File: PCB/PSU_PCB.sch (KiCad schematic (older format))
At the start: 127 parts, among them CON1 BARREL_JACK, IC1 ATMEGA328-P, P1 USB_OTG, P2 FTDI, P3 V+, P4 V-, P5 ISP, P6 I2C, P7 LCD_Display, Q1 TIP32CG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

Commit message: Small schematic fixes + added backpanel design
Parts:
- removed R37: 1.8k, Resistors_ThroughHole:Resistor_Horizontal_RM10mm, symbol R
- added D8: SS34, Diodes_SMD:D_SMB_Handsoldering, symbol D_Schottky
- D3: footprint Resistors_ThroughHole:Resistor_Horizontal_RM15mm -> Diodes_ThroughHole:D_DO-15_P15.24mm_Horizontal
- R28: value 1.8k -> 2.2k
- R39: value 1k -> 100R
- R48: value 1.8k -> 2.2k; footprint Resistors_ThroughHole:R_Axial_DIN0204_L3.6mm_D1.6mm_P7.62mm_Horizontal -> Resistors_ThroughHole:R_Axial_DIN0207_L6.3mm_D2.5mm_P10.16mm_Horizontal
- R50: value 1k -> 620R
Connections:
- net GND: now also Q2.1 (E)
- net VEE: no longer Q2.1 (E)
- net at BT1.1, R27.2, SW1.1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: now also D8.1 (K); no longer Q1.2 (C)
- new net: D8.2 (A), Q1.2 (C)
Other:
- note added: "(R50+Rpot)//R48"
- note added: "1.46 - 2.05 V"
- note added: "8 - 24 V"
- note added: "8 - 24 V\n"
- note added: "R51"
- note added: "Tab \nBAT"
- note added: "VCC max = 15 V\nTie TS to VCC/2 \nto disable temp \nmonitoring"
- note added: "Vboost=1.25(1+ )"
- note added: "__________________"
- note removed: "-3,3V"
- note removed: "1.25 - 1.75 V"
- note removed: "9 - 22 V"
- note removed: "9 - 22 V\n"
- note removed: ">650R\n<1.55K\n"
- note removed: "Off: Vout = 0 V\nVgate < 0.6 V \n"
- note removed: "VCC max = 15 V\nTie VS to VCC/2 \nto disable temp \nmonitoring"
- moved on the sheet: C24, C25, Q1, R48, R50, R51, R6, U10

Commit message: Updated BOM
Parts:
- C21: footprint Capacitors_ThroughHole:C_Disc_D3.0mm_W1.6mm_P2.50mm -> Capacitors_ThroughHole:C_Rect_L7.0mm_W2.5mm_P5.00mm
- D9: renamed from 1N4007; value D -> 1N4007
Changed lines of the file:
@@
 8E D2 4E 06 E9 83 31 0C B8 01 D4 62 7A FA FE CA 1E E7 AB A8 50 4D B8 D1 52 86 A6 EF 44 4C F7 6B
 69 A6 CB 4C 71 E1 73 B8 2B 4F 00 E7 75 28 F9 2E A2 C6 63 AC 40 DB 07 B2 19 61 39 9A 3C 4A F1 B4
-F5 AD 2E B3 0D FC 7F 6D 80 3F 3C 28 70 B1 D5 00 00 00 00 49 45 4E 44 AE 42 60 82 D3
+F5 AD 2E B3 0D FC 7F 6D 80 3F 3C 28 70 B1 D5 00 00 00 00 49 45 4E 44 AE 42 60 82 D1
 EndData
 $EndBitmap
 $Comp
-L D 1N4007
+L D D9
 U 1 1 57F00E00
 P 4200 650
-F 0 "1N4007" H 4200 750 50  0000 C CNN
-F 1 "D" H 4200 550 50  0000 C CNN
+F 0 "D9" H 4200 750 50  0000 C CNN
+F 1 "1N4007" H 4200 550 50  0000 C CNN
 F 2 "Diodes_ThroughHole:D_DO-41_SOD81_P10.16mm_Horizontal" H 4200 650 50  0001 C CNN
 F 3 "" H 4200 650 50  0000 C CNN
@@
 F 0 "C21" H 9310 5120 50  0000 L CNN
 F 1 "100n" H 9300 5000 50  0000 L CNN
-F 2 "Capacitors_ThroughHole:C_Disc_D3.0mm_W1.6mm_P2.50mm" H 9300 5050 50  0001 C CNN
+F 2 "Capacitors_ThroughHole:C_Rect_L7.0mm_W2.5mm_P5.00mm" H 9300 5050 50  0001 C CNN
 F 3 "" H 9300 5050 50  0000 C CNN
 	1    9300 5050
@@
 00 09 E8 04 41 10 04 61 00 48 40 27 08 82 20 08 03 40 02 3A 41 10 04 41 18 00 23 00 F5 5D DD 09
 82 20 08 82 20 B4 52 CF 06 60 0D 60 1C 9A D7 A4 13 04 41 10 04 D1 BD 50 00 7E F8 7F 36 C9 A5 48
-A4 FE A8 58 00 00 00 00 49 45 4E 44 AE 42 60 82 E0
+A4 FE A8 58 00 00 00 00 49 45 4E 44 AE 42 60 82 C0
 EndData
 $EndBitmap

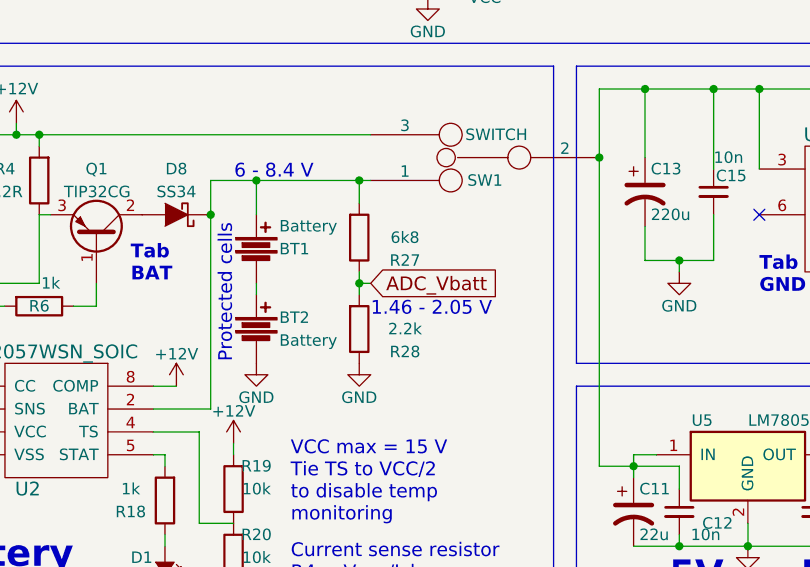
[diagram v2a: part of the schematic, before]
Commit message: Changed battery monitor resistors
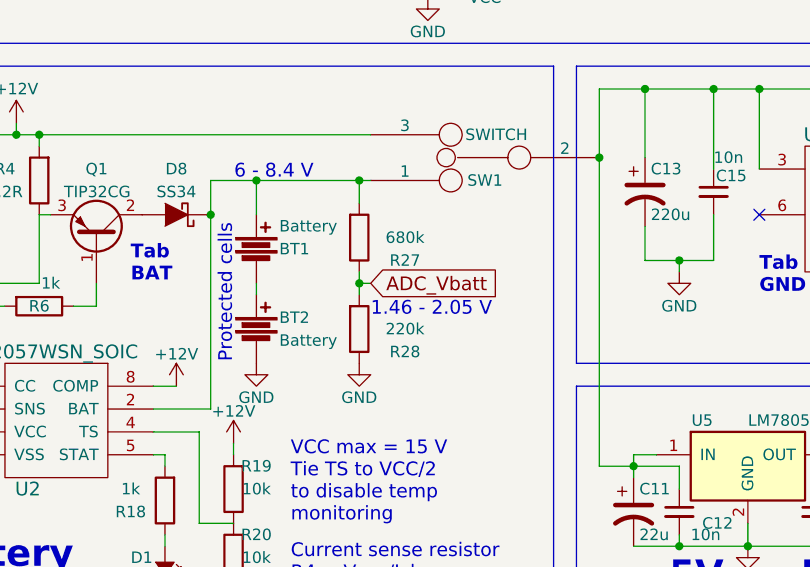
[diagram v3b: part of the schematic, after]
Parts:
- R27: value 6k8 -> 680k
- R28: value 2.2k -> 220k
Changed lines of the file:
@@
 P 2950 6350
 F 0 "R28" H 3150 6450 50  0000 C CNN
-F 1 "2.2k" H 3150 6350 50  0000 C CNN
+F 1 "220k" H 3150 6350 50  0000 C CNN
 F 2 "Resistors_ThroughHole:Resistor_Horizontal_RM10mm" V 2880 6350 50  0001 C CNN
 F 3 "" H 2950 6350 50  0000 C CNN
@@
 P 2950 5950
 F 0 "R27" H 3150 6050 50  0000 C CNN
-F 1 "6k8" H 3150 5950 50  0000 C CNN
+F 1 "680k" H 3150 5950 50  0000 C CNN
 F 2 "Resistors_ThroughHole:Resistor_Horizontal_RM10mm" V 2880 5950 50  0001 C CNN
 F 3 "" H 2950 5950 50  0000 C CNN
@@
 8E D2 4E 06 E9 83 31 0C B8 01 D4 62 7A FA FE CA 1E E7 AB A8 50 4D B8 D1 52 86 A6 EF 44 4C F7 6B
 69 A6 CB 4C 71 E1 73 B8 2B 4F 00 E7 75 28 F9 2E A2 C6 63 AC 40 DB 07 B2 19 61 39 9A 3C 4A F1 B4
-F5 AD 2E B3 0D FC 7F 6D 80 3F 3C 28 70 B1 D5 00 00 00 00 49 45 4E 44 AE 42 60 82 D1
+F5 AD 2E B3 0D FC 7F 6D 80 3F 3C 28 70 B1 D5 00 00 00 00 49 45 4E 44 AE 42 60 82 43
 EndData
 $EndBitmap
@@
 00 09 E8 04 41 10 04 61 00 48 40 27 08 82 20 08 03 40 02 3A 41 10 04 41 18 00 23 00 F5 5D DD 09
 82 20 08 82 20 B4 52 CF 06 60 0D 60 1C 9A D7 A4 13 04 41 10 04 D1 BD 50 00 7E F8 7F 36 C9 A5 48
-A4 FE A8 58 00 00 00 00 49 45 4E 44 AE 42 60 82 C0
+A4 FE A8 58 00 00 00 00 49 45 4E 44 AE 42 60 82 90
 EndData
 $EndBitmap

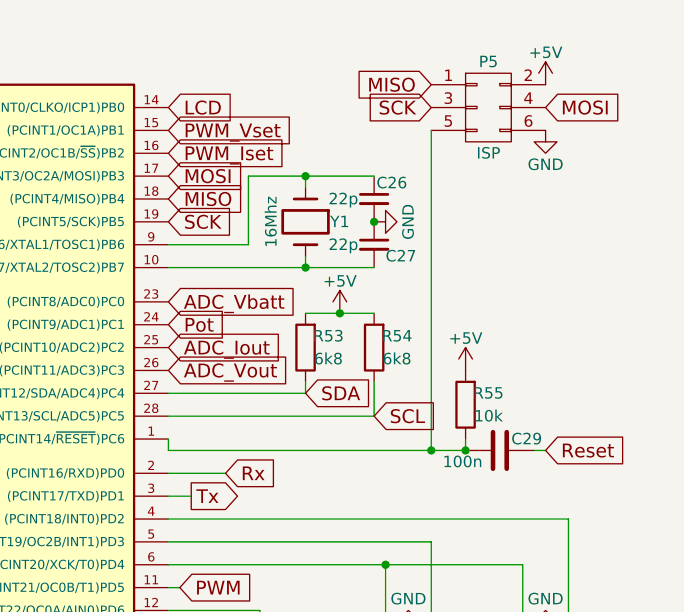
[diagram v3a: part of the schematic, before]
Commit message: Added autocalibration resistors
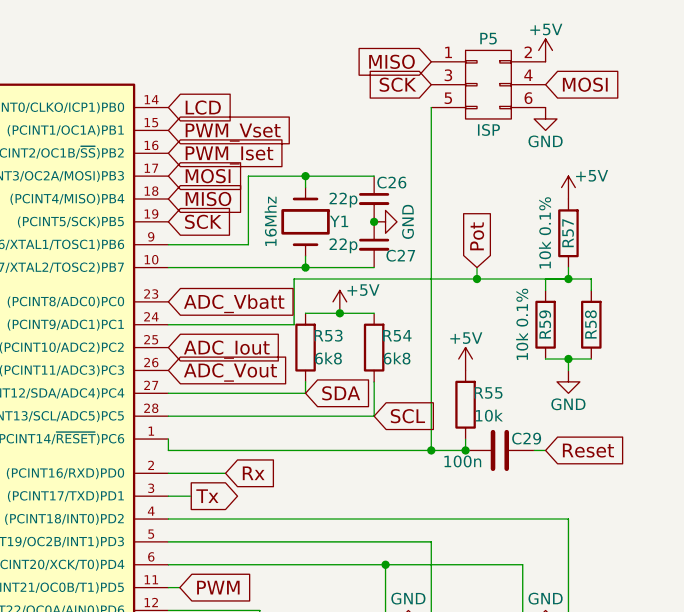
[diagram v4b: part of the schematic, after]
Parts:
- added R57, R58, R59: 10k 0.1%, Resistors_ThroughHole:R_Axial_DIN0207_L6.3mm_D2.5mm_P10.16mm_Horizontal, symbol R
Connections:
- net +5V: now also R57.2
- net GND: now also R58.1, R59.1
- net Pot: now also R57.1, R58.2, R59.2
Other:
- moved on the sheet: P5
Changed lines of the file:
@@
 P 10000 1750
 F 0 "#PWR036" H 10000 1600 50  0001 C CNN
-F 1 "+5V" H 10000 1890 50  0000 C CNN
+F 1 "+5V" H 10100 1850 50  0000 C CNN
 F 2 "" H 10000 1750 50  0000 C CNN
 F 3 "" H 10000 1750 50  0000 C CNN
@@
 L CONN_02X03 P5
 U 1 1 57BE7D24
-P 10650 850
-F 0 "P5" H 10650 1050 50  0000 C CNN
-F 1 "ISP" H 10650 650 50  0000 C CNN
-F 2 "Pin_Headers:Pin_Header_Straight_2x03" H 10650 -350 50  0001 C CNN
-F 3 "" H 10650 -350 50  0000 C CNN
-	1    10650 850
+P 10650 750
+F 0 "P5" H 10650 950 50  0000 C CNN
+F 1 "ISP" H 10650 550 50  0000 C CNN
+F 2 "Pin_Headers:Pin_Header_Straight_2x03" H 10650 -450 50  0001 C CNN
+F 3 "" H 10650 -450 50  0000 C CNN
+	1    10650 750
 	1    0    0    -1
 $EndComp
-Text GLabel 10400 750  0    60   Input ~ 0
+Text GLabel 10400 650  0    60   Input ~ 0
 MISO
-Text GLabel 10400 850  0    60   Input ~ 0
+Text GLabel 10400 750  0    60   Input ~ 0
 SCK
-Text GLabel 10900 850  2    60   Input ~ 0
+Text GLabel 10900 750  2    60   Input ~ 0
 MOSI
 $Comp
 L +5V #PWR041
 U 1 1 57BE8F13
-P 10900 750
-F 0 "#PWR041" H 10900 600 50  0001 C CNN
-F 1 "+5V" H 10900 890 50  0000 C CNN
-F 2 "" H 10900 750 50  0000 C CNN
-F 3 "" H 10900 750 50  0000 C CNN
-	1    10900 750
+P 10900 650
+F 0 "#PWR041" H 10900 500 50  0001 C CNN
+F 1 "+5V" H 10900 790 50  0000 C CNN
+F 2 "" H 10900 650 50  0000 C CNN
+F 3 "" H 10900 650 50  0000 C CNN
+	1    10900 650
 	1    0    0    -1
 $EndComp
@@
 L GND #PWR042
 U 1 1 57BE944C
-P 10900 950
-F 0 "#PWR042" H 10900 700 50  0001 C CNN
-F 1 "GND" H 10900 800 50  0000 C CNN
-F 2 "" H 10900 950 50  0000 C CNN
-F 3 "" H 10900 950 50  0000 C CNN
-	1    10900 950
+P 10900 850
+F 0 "#PWR042" H 10900 600 50  0001 C CNN
+F 1 "GND" H 10900 700 50  0000 C CNN
+F 2 "" H 10900 850 50  0000 C CNN
+F 3 "" H 10900 850 50  0000 C CNN
+	1    10900 850
 	1    0    0    -1
 $EndComp
@@
 NoConn ~ 6300 5950
 NoConn ~ 4650 1200
-Text GLabel 9250 1800 2    60   Input ~ 0
+Text GLabel 10600 1550 1    60   Input ~ 0
 Pot
 Text GLabel 7100 5950 2    60   Input ~ 0
@@
 8E D2 4E 06 E9 83 31 0C B8 01 D4 62 7A FA FE CA 1E E7 AB A8 50 4D B8 D1 52 86 A6 EF 44 4C F7 6B
 69 A6 CB 4C 71 E1 73 B8 2B 4F 00 E7 75 28 F9 2E A2 C6 63 AC 40 DB 07 B2 19 61 39 9A 3C 4A F1 B4
-F5 AD 2E B3 0D FC 7F 6D 80 3F 3C 28 70 B1 D5 00 00 00 00 49 45 4E 44 AE 42 60 82 43
+F5 AD 2E B3 0D FC 7F 6D 80 3F 3C 28 70 B1 D5 00 00 00 00 49 45 4E 44 AE 42 60 82 3E
 EndData
 $EndBitmap
@@
 00 09 E8 04 41 10 04 61 00 48 40 27 08 82 20 08 03 40 02 3A 41 10 04 41 18 00 23 00 F5 5D DD 09
 82 20 08 82 20 B4 52 CF 06 60 0D 60 1C 9A D7 A4 13 04 41 10 04 D1 BD 50 00 7E F8 7F 36 C9 A5 48
-A4 FE A8 58 00 00 00 00 49 45 4E 44 AE 42 60 82 90
+A4 FE A8 58 00 00 00 00 49 45 4E 44 AE 42 60 82 D0
 EndData
 $EndBitmap
@@
 Connection ~ 10400 2350
 Wire Wire Line
-	10400 950  10400 2350
+	10400 850  10400 2350
 Wire Wire Line
 	9250 2350 9250 2300
@@
 Text Notes 7550 6300 0    60   ~ 0
 __________________
+$Comp
+L R R57
+U 1 1 58F0CBED
+P 11000 1400
+F 0 "R57" V 11000 1400 50  0000 C CNN
+F 1 "10k 0.1%" V 11100 1400 50  0000 C CNN
+F 2 "Resistors_ThroughHole:R_Axial_DIN0207_L6.3mm_D2.5mm_P10.16mm_Horizontal" V 10930 1400 50  0001 C CNN
+F 3 "" H 11000 1400 50  0000 C CNN
+	1    11000 1400
+	-1   0    0    1
+$EndComp
+$Comp
+L R R59
+U 1 1 58F0CDAA
+P 10900 1800
+F 0 "R59" V 10900 1800 50  0000 C CNN
+F 1 "10k 0.1%" V 11000 1800 50  0000 C CNN
+F 2 "Resistors_ThroughHole:R_Axial_DIN0207_L6.3mm_D2.5mm_P10.16mm_Horizontal" V 10830 1800 50  0001 C CNN
+F 3 "" H 10900 1800 50  0000 C CNN
+	1    10900 1800
+	-1   0    0    1
+$EndComp
+$Comp
+L R R58
+U 1 1 58F0CFF6
+P 11100 1800
+F 0 "R58" V 11100 1800 50  0000 C CNN
+F 1 "10k 0.1%" H 10850 1900 50  0001 C CNN
+F 2 "Resistors_ThroughHole:R_Axial_DIN0207_L6.3mm_D2.5mm_P10.16mm_Horizontal" V 11030 1800 50  0001 C CNN
+F 3 "" H 11100 1800 50  0000 C CNN
+	1    11100 1800
+	-1   0    0    1
+$EndComp
+$Comp
+L GND #PWR081
+U 1 1 58F14CCC
+P 11000 2000
+F 0 "#PWR081" H 11000 1750 50  0001 C CNN
+F 1 "GND" H 11000 1850 50  0000 C CNN
+F 2 "" H 11000 2000 50  0000 C CNN
+F 3 "" H 11000 2000 50  0000 C CNN
+	1    11000 2000
+	1    0    0    -1
+$EndComp
+$Comp
+L +5V #PWR082
+U 1 1 58F17B68
+P 11000 1250
+F 0 "#PWR082" H 11000 1100 50  0001 C CNN
+F 1 "+5V" H 11100 1350 50  0000 C CNN
+F 2 "" H 11000 1250 50  0000 C CNN
+F 3 "" H 11000 1250 50  0000 C CNN
+	1    11000 1250
+	1    0    0    -1
+$EndComp
+Wire Wire Line
+	10900 1950 11100 1950
+Wire Wire Line
+	11000 2000 11000 1950
+Connection ~ 11000 1950
+Wire Wire Line
+	9250 1800 9800 1800
+Wire Wire Line
+	9800 1800 9800 1600
+Wire Wire Line
+	9800 1600 11100 1600
+Wire Wire Line
+	11000 1600 11000 1550
+Wire Wire Line
+	11100 1600 11100 1650
+Connection ~ 11000 1600
+Wire Wire Line
+	10900 1650 10900 1600
+Wire Wire Line
+	10900 1600 11000 1600
+Wire Wire Line
+	10600 1550 10600 1600
+Connection ~ 10600 1600
 $EndSCHEMATC

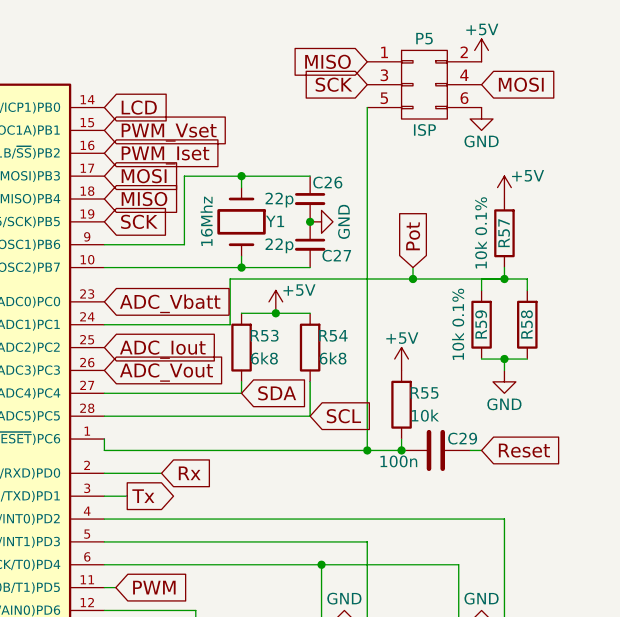
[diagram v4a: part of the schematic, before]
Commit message: Added auto calibration
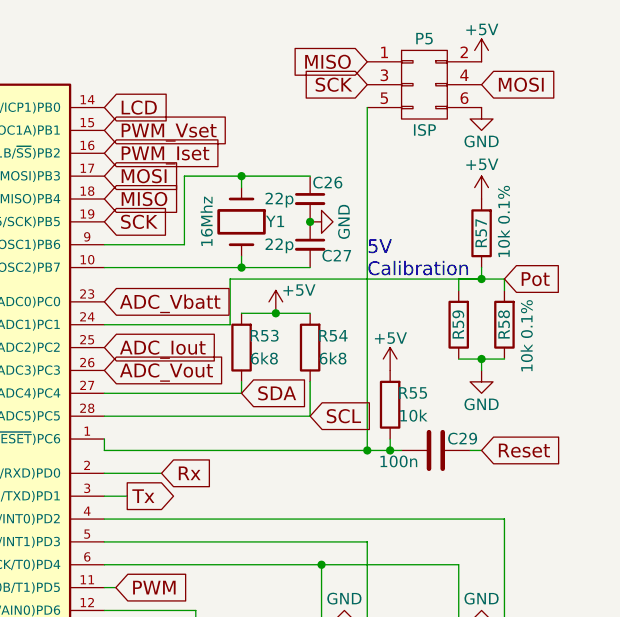
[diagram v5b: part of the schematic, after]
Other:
- note added: "5V \nCalibration"
- moved on the sheet: R55, R57, R58, R59
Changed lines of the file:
@@
 L R R55
 U 1 1 57BDF708
-P 10550 2150
-F 0 "R55" H 10450 2100 50  0000 C CNN
-F 1 "10k" H 10450 2200 50  0000 C CNN
-F 2 "Resistors_ThroughHole:Resistor_Horizontal_RM10mm" V 10480 2150 50  0001 C CNN
-F 3 "" H 10550 2150 50  0000 C CNN
-	1    10550 2150
+P 10500 2150
+F 0 "R55" H 10400 2100 50  0000 C CNN
+F 1 "10k" H 10400 2200 50  0000 C CNN
+F 2 "Resistors_ThroughHole:Resistor_Horizontal_RM10mm" V 10430 2150 50  0001 C CNN
+F 3 "" H 10500 2150 50  0000 C CNN
+	1    10500 2150
 	-1   0    0    1
 $EndComp
@@
 L +5V #PWR040
 U 1 1 57BDFADC
-P 10550 2000
-F 0 "#PWR040" H 10550 1850 50  0001 C CNN
-F 1 "+5V" H 10550 2140 50  0000 C CNN
-F 2 "" H 10550 2000 50  0000 C CNN
-F 3 "" H 10550 2000 50  0000 C CNN
-	1    10550 2000
+P 10500 2000
+F 0 "#PWR040" H 10500 1850 50  0001 C CNN
+F 1 "+5V" H 10500 2140 50  0000 C CNN
+F 2 "" H 10500 2000 50  0000 C CNN
+F 3 "" H 10500 2000 50  0000 C CNN
+	1    10500 2000
 	1    0    0    -1
 $EndComp
@@
 NoConn ~ 6300 5950
 NoConn ~ 4650 1200
-Text GLabel 10600 1550 1    60   Input ~ 0
+Text GLabel 11000 1600 2    60   Input ~ 0
 Pot
 Text GLabel 7100 5950 2    60   Input ~ 0
@@
 8E D2 4E 06 E9 83 31 0C B8 01 D4 62 7A FA FE CA 1E E7 AB A8 50 4D B8 D1 52 86 A6 EF 44 4C F7 6B
 69 A6 CB 4C 71 E1 73 B8 2B 4F 00 E7 75 28 F9 2E A2 C6 63 AC 40 DB 07 B2 19 61 39 9A 3C 4A F1 B4
-F5 AD 2E B3 0D FC 7F 6D 80 3F 3C 28 70 B1 D5 00 00 00 00 49 45 4E 44 AE 42 60 82 3E
+F5 AD 2E B3 0D FC 7F 6D 80 3F 3C 28 70 B1 D5 00 00 00 00 49 45 4E 44 AE 42 60 82 A3
 EndData
 $EndBitmap
@@
 00 09 E8 04 41 10 04 61 00 48 40 27 08 82 20 08 03 40 02 3A 41 10 04 41 18 00 23 00 F5 5D DD 09
 82 20 08 82 20 B4 52 CF 06 60 0D 60 1C 9A D7 A4 13 04 41 10 04 D1 BD 50 00 7E F8 7F 36 C9 A5 48
-A4 FE A8 58 00 00 00 00 49 45 4E 44 AE 42 60 82 D0
+A4 FE A8 58 00 00 00 00 49 45 4E 44 AE 42 60 82 50
 EndData
 $EndBitmap
@@
 Connection ~ 650  3800
 Connection ~ 1000 3800
-Connection ~ 10550 2350
-Wire Wire Line
-	10550 2300 10550 2350
 Wire Wire Line
 	4650 3600 4650 3650
@@
 Connection ~ 10400 2350
 Wire Wire Line
-	10400 850  10400 2350
-Wire Wire Line
 	9250 2350 9250 2300
 Wire Wire Line
@@
 L R R57
 U 1 1 58F0CBED
-P 11000 1400
-F 0 "R57" V 11000 1400 50  0000 C CNN
-F 1 "10k 0.1%" V 11100 1400 50  0000 C CNN
-F 2 "Resistors_ThroughHole:R_Axial_DIN0207_L6.3mm_D2.5mm_P10.16mm_Horizontal" V 10930 1400 50  0001 C CNN
-F 3 "" H 11000 1400 50  0000 C CNN
-	1    11000 1400
+P 10900 1400
+F 0 "R57" V 10900 1400 50  0000 C CNN
+F 1 "10k 0.1%" V 10800 1350 50  0000 C CNN
+F 2 "Resistors_ThroughHole:R_Axial_DIN0207_L6.3mm_D2.5mm_P10.16mm_Horizontal" V 10830 1400 50  0001 C CNN
+F 3 "" H 10900 1400 50  0000 C CNN
+	1    10900 1400
 	-1   0    0    1
 $EndComp
@@
 L R R59
 U 1 1 58F0CDAA
-P 10900 1800
-F 0 "R59" V 10900 1800 50  0000 C CNN
-F 1 "10k 0.1%" V 11000 1800 50  0000 C CNN
-F 2 "Resistors_ThroughHole:R_Axial_DIN0207_L6.3mm_D2.5mm_P10.16mm_Horizontal" V 10830 1800 50  0001 C CNN
-F 3 "" H 10900 1800 50  0000 C CNN
-	1    10900 1800
+P 10800 1800
+F 0 "R59" V 10800 1800 50  0000 C CNN
+F 1 "10k 0.1%" V 10500 1850 50  0000 C CNN
+F 2 "Resistors_ThroughHole:R_Axial_DIN0207_L6.3mm_D2.5mm_P10.16mm_Horizontal" V 10730 1800 50  0001 C CNN
+F 3 "" H 10800 1800 50  0000 C CNN
+	1    10800 1800
 	-1   0    0    1
 $EndComp
@@
 L R R58
 U 1 1 58F0CFF6
-P 11100 1800
-F 0 "R58" V 11100 1800 50  0000 C CNN
-F 1 "10k 0.1%" H 10850 1900 50  0001 C CNN
-F 2 "Resistors_ThroughHole:R_Axial_DIN0207_L6.3mm_D2.5mm_P10.16mm_Horizontal" V 11030 1800 50  0001 C CNN
-F 3 "" H 11100 1800 50  0000 C CNN
-	1    11100 1800
+P 11000 1800
+F 0 "R58" V 11000 1800 50  0000 C CNN
+F 1 "10k 0.1%" H 10750 1900 50  0001 C CNN
+F 2 "Resistors_ThroughHole:R_Axial_DIN0207_L6.3mm_D2.5mm_P10.16mm_Horizontal" V 10930 1800 50  0001 C CNN
+F 3 "" H 11000 1800 50  0000 C CNN
+	1    11000 1800
 	-1   0    0    1
 $EndComp
@@
 L GND #PWR081
 U 1 1 58F14CCC
-P 11000 2000
-F 0 "#PWR081" H 11000 1750 50  0001 C CNN
-F 1 "GND" H 11000 1850 50  0000 C CNN
-F 2 "" H 11000 2000 50  0000 C CNN
-F 3 "" H 11000 2000 50  0000 C CNN
-	1    11000 2000
+P 10900 2000
+F 0 "#PWR081" H 10900 1750 50  0001 C CNN
+F 1 "GND" H 10900 1850 50  0000 C CNN
+F 2 "" H 10900 2000 50  0000 C CNN
+F 3 "" H 10900 2000 50  0000 C CNN
+	1    10900 2000
 	1    0    0    -1
 $EndComp
@@
 L +5V #PWR082
 U 1 1 58F17B68
-P 11000 1250
-F 0 "#PWR082" H 11000 1100 50  0001 C CNN
-F 1 "+5V" H 11100 1350 50  0000 C CNN
-F 2 "" H 11000 1250 50  0000 C CNN
-F 3 "" H 11000 1250 50  0000 C CNN
-	1    11000 1250
+P 10900 1250
+F 0 "#PWR082" H 10900 1100 50  0001 C CNN
+F 1 "+5V" H 10900 1400 50  0000 C CNN
+F 2 "" H 10900 1250 50  0000 C CNN
+F 3 "" H 10900 1250 50  0000 C CNN
+	1    10900 1250
 	1    0    0    -1
 $EndComp
 Wire Wire Line
-	10900 1950 11100 1950
+	10800 1950 11000 1950
 Wire Wire Line
-	11000 2000 11000 1950
-Connection ~ 11000 1950
+	10900 2000 10900 1950
+Connection ~ 10900 1950
 Wire Wire Line
 	9250 1800 9800 1800
@@
 	9800 1800 9800 1600
 Wire Wire Line
-	9800 1600 11100 1600
+	10400 850  10400 2350
+Wire Wire Line
+	10500 2300 10500 2350
+Connection ~ 10500 2350
+Connection ~ 10900 1600
 Wire Wire Line
-	11000 1600 11000 1550
+	10800 1600 10900 1600
 Wire Wire Line
-	11100 1600 11100 1650
-Connection ~ 11000 1600
+	10900 1600 10900 1550
 Wire Wire Line
-	10900 1650 10900 1600
+	11000 1600 11000 1650
 Wire Wire Line
-	10900 1600 11000 1600
+	10800 1650 10800 1600
 Wire Wire Line
-	10600 1550 10600 1600
-Connection ~ 10600 1600
+	9800 1600 11000 1600
+Text Notes 10400 1600 0    60   ~ 0
+    5V \nCalibration
 $EndSCHEMATC
